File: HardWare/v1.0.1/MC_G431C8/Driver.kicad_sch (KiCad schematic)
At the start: 74 parts, among them J5 Conn_01x03, U2 fd6288t, U3 LMV324I, U8 AS5047D

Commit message: 20240606 01:01 硬件:电源布局完成
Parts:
- R29: footprint Resistor_SMD:R_2512_6332Metric -> Resistor_SMD:R_0603_1608Metric_Pad0.98x0.95mm_HandSolder
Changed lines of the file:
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@@
 			)
 		)
-		(property "Footprint" "Resistor_SMD:R_2512_6332Metric"
+		(property "Footprint" "Resistor_SMD:R_0603_1608Metric_Pad0.98x0.95mm_HandSolder"
 			(at 64.516 173.736 90)
 			(effects

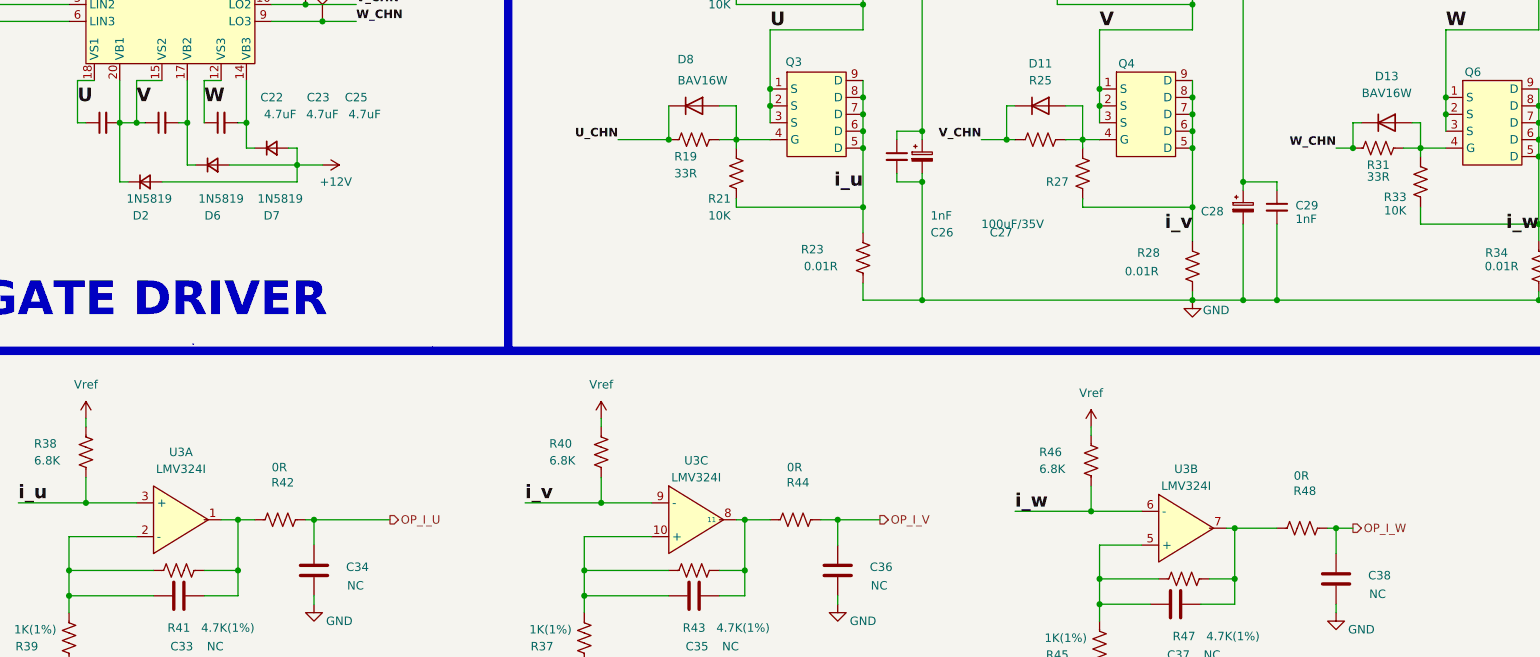
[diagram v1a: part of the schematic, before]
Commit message: 20240610 硬件布局完成95%，软件增加速度环
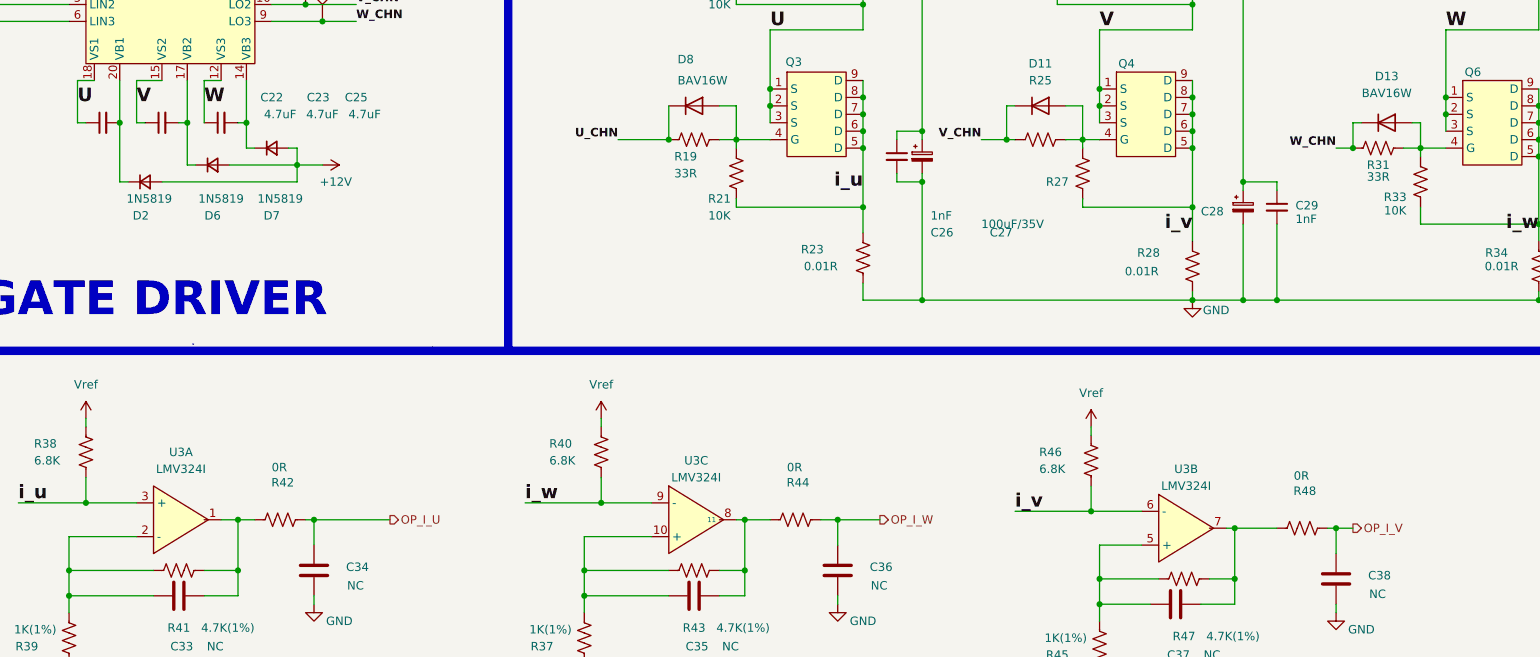
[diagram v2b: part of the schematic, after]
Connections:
- net OP_I_V: now also C38.2, R48.2; no longer C36.2, R44.2
- net OP_I_W: now also C36.2, R44.2; no longer C38.2, R48.2
- net V: no longer C22.2, D2.1 (K), U2.20 (VB1)
- net i_v: now also R46.2, U3.6 (-); no longer R40.2, U3.9 (-)
- net i_w: now also R40.2, U3.9 (-); no longer R46.2, U3.6 (-)
- new net: C22.2, D2.1 (K), U2.20 (VB1)
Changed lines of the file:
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@@
 	)
 	(junction
-		(at 43.18 62.23)
-		(diameter 0)
-		(color 0 0 0 0)
-	)
-	(junction
 		(at 138.43 57.15)
 		(diameter 0)
@@
 	(wire
 		(pts
-			(xy 40.64 62.23) (xy 43.18 62.23)
-		)
-		(stroke
-			(width 0)
-			(type default)
-		)
-	)
-	(wire
-		(pts
 			(xy 181.61 44.45) (xy 201.93 44.45)
 		)
@@
 	)
 	(label "i_v"
-		(at 101.6 119.38 0)
+		(at 175.26 120.65 0)
 		(fields_autoplaced yes)
 		(effects
@@
 	)
 	(label "i_w"
-		(at 175.26 120.65 0)
+		(at 101.6 119.38 0)
 		(fields_autoplaced yes)
 		(effects
@@
 	(hierarchical_label "OP_I_V"
 		(shape output)
-		(at 154.94 121.92 0)
+		(at 226.06 123.19 0)
 		(fields_autoplaced yes)
 		(effects
@@
 	(hierarchical_label "OP_I_W"
 		(shape output)
-		(at 226.06 123.19 0)
+		(at 154.94 121.92 0)
 		(fields_autoplaced yes)
 		(effects
